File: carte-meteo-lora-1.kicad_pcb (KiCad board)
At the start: 2 copper layers, 60 x 45 mm, 121 parts, among them J1 TC2030, J2 Conn_01x04, J3 Conn_01x04, J4 Conn_Coaxial, J5 USB_C_Receptacle_USB2.0_14P, J6 Solar_Cell, J7 Conn_01x02, J8 Battery_Cell, Q1 AO4882, Q2 AO4882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

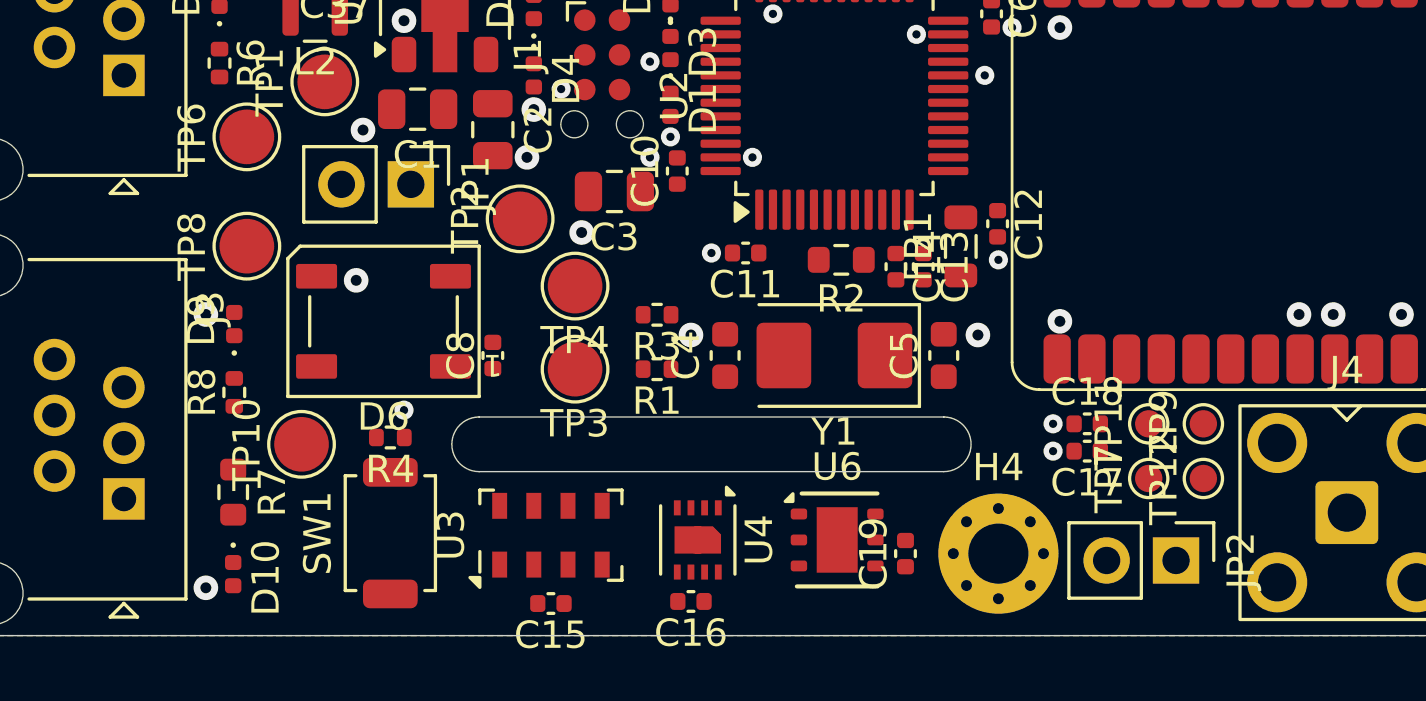
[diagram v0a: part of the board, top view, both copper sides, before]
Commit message: pcb: reorganize programmable gpios
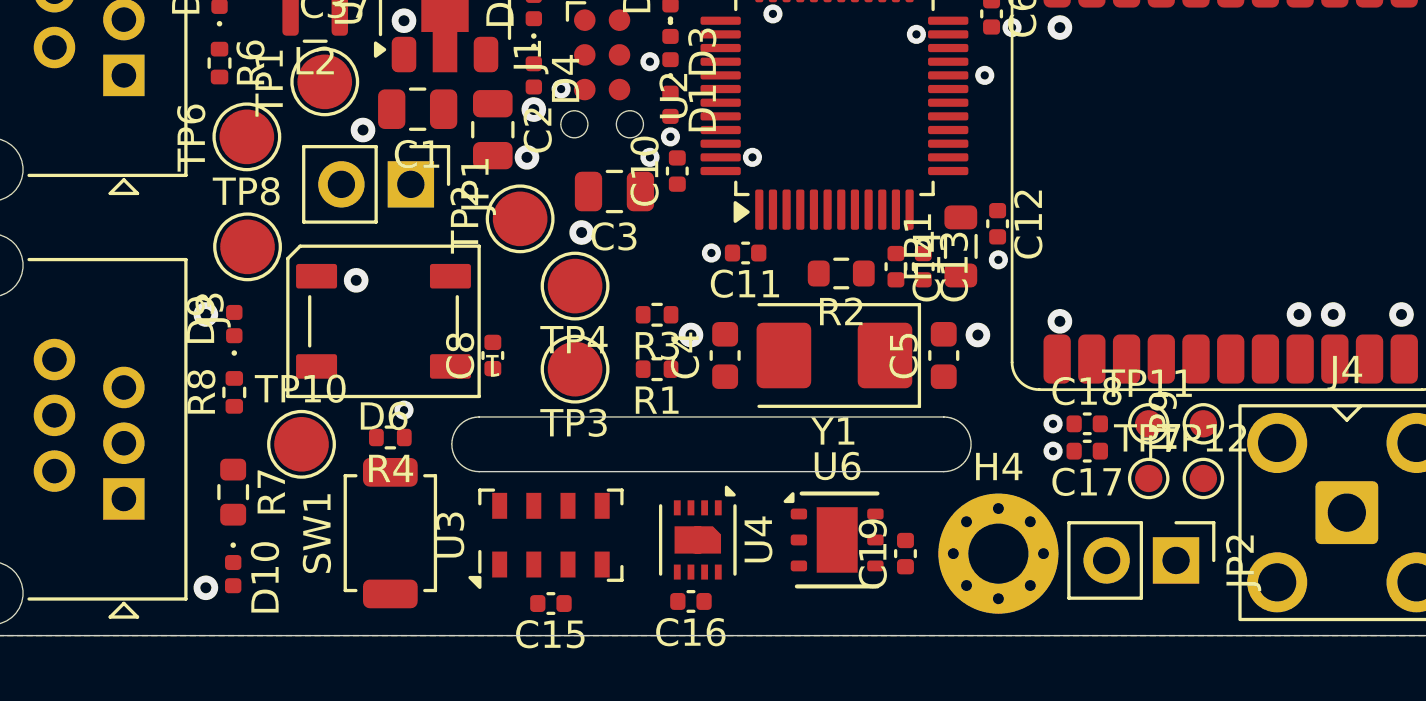
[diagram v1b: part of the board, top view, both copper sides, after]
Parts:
- moved R2 0.50 mm to (87.2, 54.8)
- turned TP8 to 0 degrees
- turned TP10 to 0 degrees
- turned TP11 to 0 degrees
- turned TP12 to 0 degrees
- turned TP7 to 0 degrees
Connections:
- R5 pad 1: Net-(U2-PA15) -> Net-(U2-PB12)
- U2 pad 10: /RAIN -> /WIND
- U2 pad 11: /SCK -> /W_DIR
- U2 pad 12: /WIND -> /ALERT
- U2 pad 15: /W_DIR -> /SCK
- U2 pad 16: /RGB1 -> /MISO
- U2 pad 17: unconnected-(U2-PA7-Pad17) -> /MOSI
- U2 pad 18: unconnected-(U2-PB0-Pad18) -> /RST
- U2 pad 19: unconnected-(U2-PB1-Pad19) -> /DIO1
- U2 pad 2: unconnected-(U2-PC13-Pad2) -> /RGB1
- U2 pad 21: /Power/~{CE} -> /DIO3
- U2 pad 22: unconnected-(U2-PB11-Pad22) -> /BUSY
- U2 pad 25: /RST -> Net-(U2-PB12)
- U2 pad 26: /DIO3 -> /BTN1
- U2 pad 27: /DIO1 -> unconnected-(U2-PB14-Pad27)
- U2 pad 28: /BUSY -> unconnected-(U2-PB15-Pad28)
- U2 pad 30: /ALERT -> unconnected-(U2-PA9-Pad30)
- U2 pad 31: unconnected-(U2-PA10-Pad31) -> /Power/~{QON}
- U2 pad 32: /MISO -> /Power/~{CE}
- U2 pad 33: /MOSI -> /Power/~{INT}
- U2 pad 38: Net-(U2-PA15) -> unconnected-(U2-PA15-Pad38)
- U2 pad 40: unconnected-(U2-PB4-Pad40) -> /RAIN
- U2 pad 41: /BTN1 -> unconnected-(U2-PB5-Pad41)
- U2 pad 45: /Power/~{QON} -> unconnected-(U2-PB8-Pad45)
- U2 pad 46: /Power/~{INT} -> unconnected-(U2-PB9-Pad46)

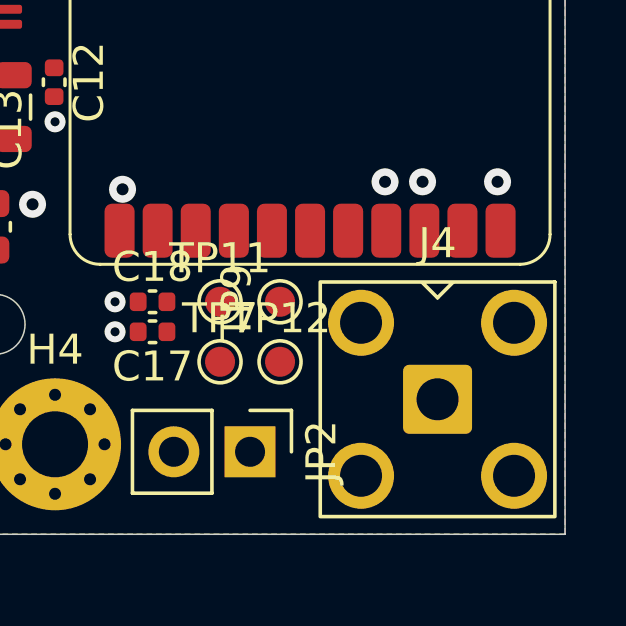
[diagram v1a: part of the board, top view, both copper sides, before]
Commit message: pcb: add rf routing
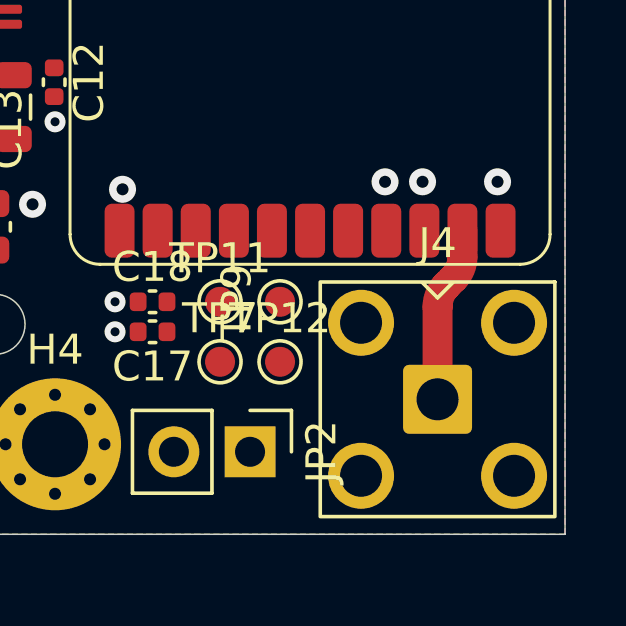
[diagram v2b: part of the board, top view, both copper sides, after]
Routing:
- net /RF_LR: track 0.00 -> 5.87 mm
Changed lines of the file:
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@@
 		(net "GND")
+	)
+	(segment
+		(start 106.58 57.88)
+		(end 106.58 58.755786)
+		(width 1)
+		(layer "F.Cu")
+		(net "/RF_LR")
+	)
+	(segment
+		(start 105.75 60.414172)
+		(end 105.75 63.5)
+		(width 1)
+		(layer "F.Cu")
+		(net "/RF_LR")
+	)
+	(segment
+		(start 106.287138 59.462862)
+		(end 106.042893 59.707107)
+		(width 1)
+		(layer "F.Cu")
+		(net "/RF_LR")
+	)
+	(arc
+		(start 106.287138 59.462862)
+		(mid 106.503891 59.138465)
+		(end 106.58 58.755786)
+		(width 1)
+		(layer "F.Cu")
+		(net "/RF_LR")
+	)
+	(arc
+		(start 106.042893 59.707107)
+		(mid 105.826125 60.031498)
+		(end 105.75 60.414172)
+		(width 1)
+		(layer "F.Cu")
+		(net "/RF_LR")
 	)
 	(zone

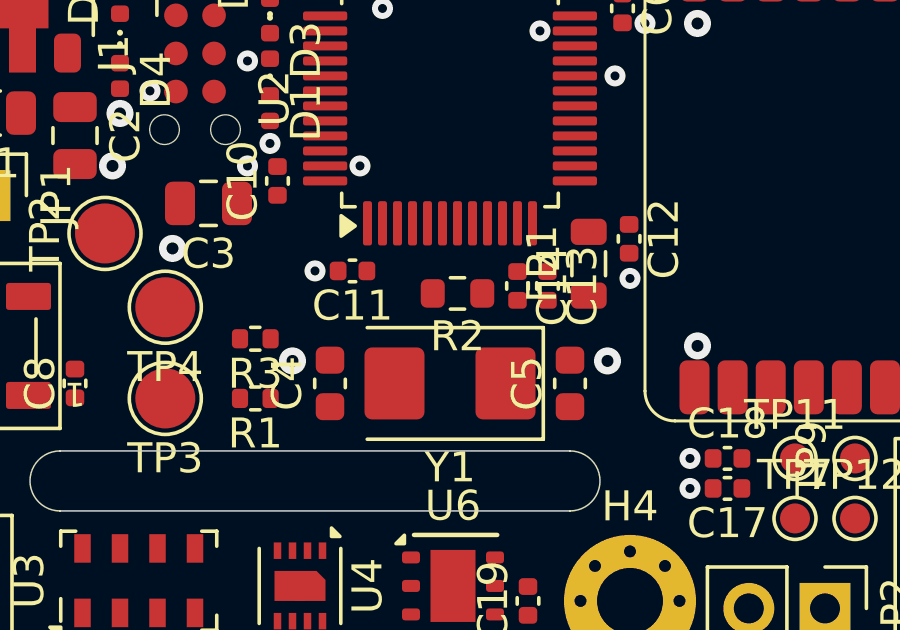
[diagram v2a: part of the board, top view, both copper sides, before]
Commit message: pcb: add xtal routing
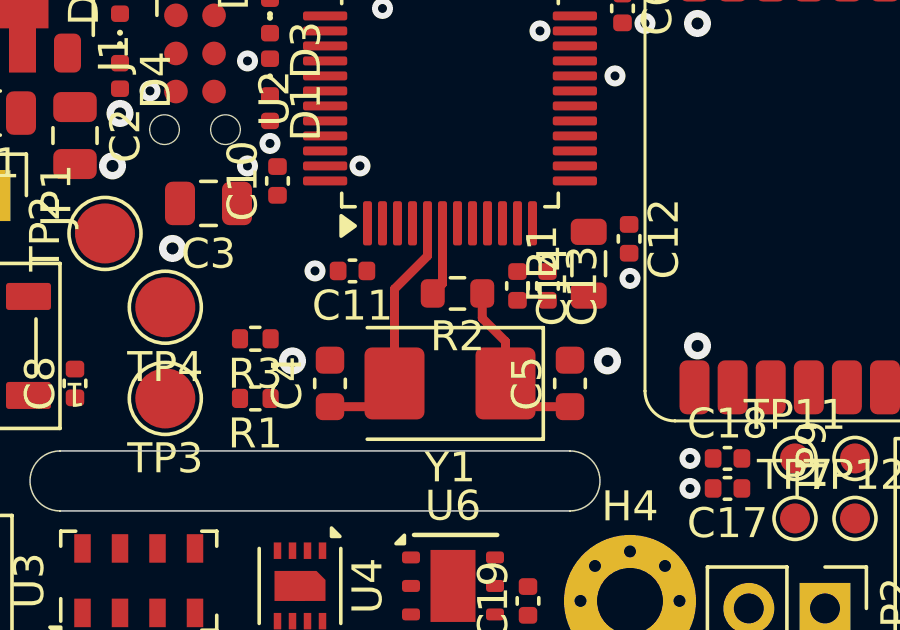
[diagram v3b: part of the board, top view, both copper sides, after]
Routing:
- net /XTAL_I: track 0.00 -> 8.26 mm
- net /XTAL_RO: track 0.00 -> 5.79 mm
- net /XTAL_O: track 0.00 -> 2.47 mm
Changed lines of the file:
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@@
+	)
+	(segment
+		(start 88.85 57.75)
+		(end 88.85 56.35)
+		(width 0.3)
+		(layer "F.Cu")
+		(net "/XTAL_RO")
+	)
+	(segment
+		(start 88.85 56.35)
+		(end 88.075 55.575)
+		(width 0.3)
+		(layer "F.Cu")
+		(net "/XTAL_RO")
+	)
+	(segment
+		(start 88.075 55.575)
+		(end 88.075 54.75)
+		(width 0.3)
+		(layer "F.Cu")
+		(net "/XTAL_RO")
+	)
+	(segment
+		(start 89.625 58.525)
+		(end 88.85 57.75)
+		(width 0.3)
+		(layer "F.Cu")
+		(net "/XTAL_RO")
+	)
+	(segment
+		(start 91 58.525)
+		(end 89.625 58.525)
+		(width 0.3)
+		(layer "F.Cu")
+		(net "/XTAL_RO")
 	)
 	(segment
@@
 	)
 	(segment
+		(start 83 58.525)
+		(end 84.375 58.525)
+		(width 0.3)
+		(layer "F.Cu")
+		(net "/XTAL_I")
+	)
+	(segment
+		(start 84.375 58.525)
+		(end 85.15 57.75)
+		(width 0.3)
+		(layer "F.Cu")
+		(net "/XTAL_I")
+	)
+	(segment
+		(start 86.25 52.4125)
+		(end 86.25 53.5)
+		(width 0.3)
+		(layer "F.Cu")
+		(net "/XTAL_I")
+	)
+	(segment
+		(start 86.25 53.5)
+		(end 85.15 54.6)
+		(width 0.3)
+		(layer "F.Cu")
+		(net "/XTAL_I")
+	)
+	(segment
+		(start 85.15 54.6)
+		(end 85.15 57.75)
+		(width 0.3)
+		(layer "F.Cu")
+		(net "/XTAL_I")
+	)
+	(segment
+		(start 86.75 52.4125)
+		(end 86.75 54.425)
+		(width 0.3)
+		(layer "F.Cu")
+		(net "/XTAL_O")
+	)
+	(segment
+		(start 86.75 54.425)
+		(end 86.425 54.75)
+		(width 0.3)
+		(layer "F.Cu")
+		(net "/XTAL_O")
+	)
+	(segment

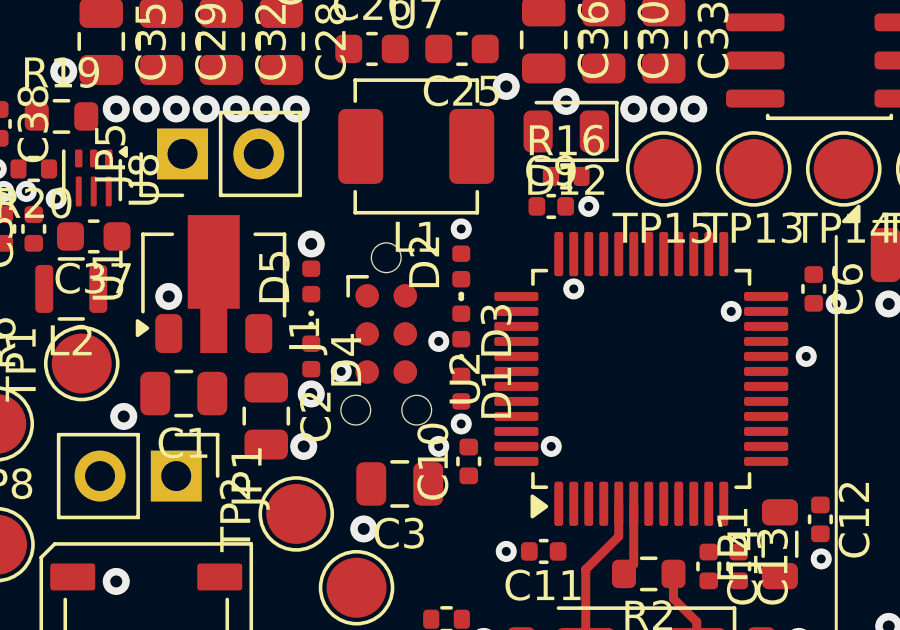
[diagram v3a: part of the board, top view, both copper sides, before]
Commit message: pcb: add swd routing
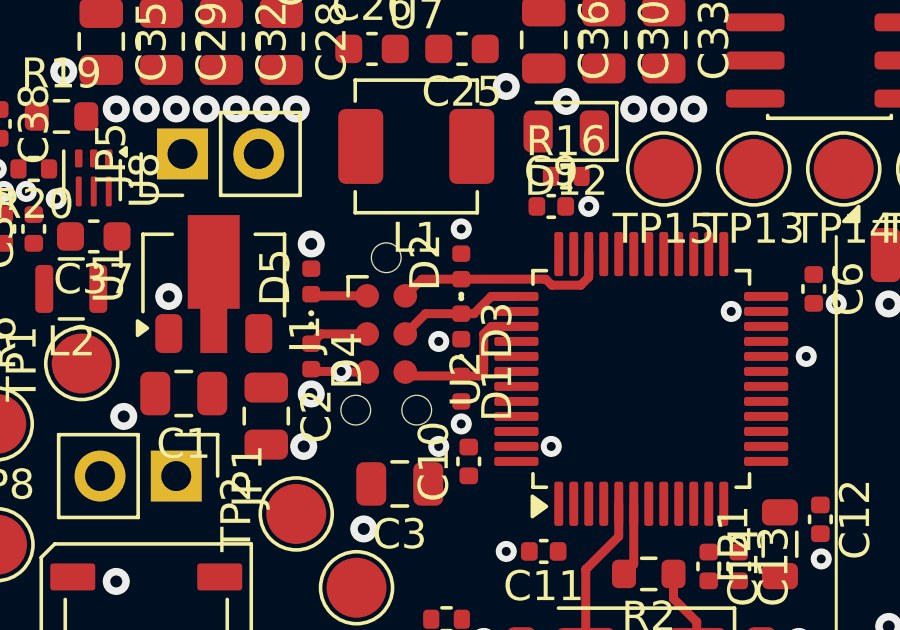
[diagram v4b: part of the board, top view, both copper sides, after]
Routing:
- net /SWDIO: track 0.00 -> 7.31 mm
- net /SWO: track 0.00 -> 5.17 mm
- net /SWCLK: track 0.00 -> 4.22 mm
- net /NRST: track 0.00 -> 2.00 mm
- net GND: track 1.45 -> 3.36 mm, vias 73 -> 72
- net +3V3: track 0.00 -> 1.89 mm
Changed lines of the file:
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@@
+	)
+	(segment
+		(start 76.075 48)
+		(end 76 47.925)
+		(width 0.3)
+		(layer "F.Cu")
+		(net "GND")
 	)
 	(segment
@@
 	)
 	(segment
+		(start 77.02 48.02)
+		(end 77 48)
+		(width 0.3)
+		(layer "F.Cu")
+		(net "GND")
+	)
+	(segment
+		(start 77 48)
+		(end 76.075 48)
+		(width 0.3)
+		(layer "F.Cu")
+		(net "GND")
+	)
+	(segment
 		(start 76.96 27.75)
 		(end 77 27.75)
@@
 		(net "GND")
 	)
+	(segment
+		(start 77.865 48.02)
+		(end 77.02 48.02)
+		(width 0.3)
+		(layer "F.Cu")
+		(net "GND")
+	)
 	(via
 		(at 100.18 29.51)
@@
 	)
 	(via
-		(at 84.75 45.25)
-		(size 0.7)
-		(drill 0.3)
-		(layers "F.Cu" "B.Cu")
-		(free yes)
-		(net "GND")
-	)
-	(via
 		(at 80.25 47)
 		(size 0.7)
@@
 		(free yes)
 		(net "GND")
+	)
+	(segment
+		(start 76.055 45.48)
+		(end 76 45.425)
+		(width 0.3)
+		(layer "F.Cu")
+		(net "+3V3")
+	)
+	(segment
+		(start 77.865 45.48)
+		(end 76.055 45.48)
+		(width 0.3)
+		(layer "F.Cu")
+		(net "+3V3")
+	)
+	(segment
+		(start 82.8375 45.5)
+		(end 82 45.5)
+		(width 0.3)
+		(layer "F.Cu")
+		(net "/SWCLK")
+	)
+	(segment
+		(start 79.81 46.075)
+		(end 79.135 46.75)
+		(width 0.3)
+		(layer "F.Cu")
+		(net "/SWCLK")
+	)
+	(segment
+		(start 82 45.5)
+		(end 81.425 46.075)
+		(width 0.3)
+		(layer "F.Cu")
+		(net "/SWCLK")
+	)
+	(segment
+		(start 81.425 46.075)
+		(end 81 46.075)
+		(width 0.3)
+		(layer "F.Cu")
+		(net "/SWCLK")
+	)
+	(segment
+		(start 81 46.075)
+		(end 79.81 46.075)
+		(width 0.3)
+		(layer "F.Cu")
+		(net "/SWCLK")
 	)
 	(segment
@@
 	)
 	(segment
+		(start 76.325 46.75)
+		(end 76 47.075)
+		(width 0.3)
+		(layer "F.Cu")
+		(net "/NRST")
+	)
+	(segment
+		(start 77.865 46.75)
+		(end 76.325 46.75)
+		(width 0.3)
+		(layer "F.Cu")
+		(net "/NRST")
+	)
+	(segment
+		(start 81 44.925)
+		(end 79.69 44.925)
+		(width 0.3)
+		(layer "F.Cu")
+		(net "/SWDIO")
+	)
+	(segment
+		(start 83.81759 44.925)
+		(end 84.01759 45.125)
+		(width 0.3)
+		(layer "F.Cu")
+		(net "/SWDIO")
+	)
+	(segment
+		(start 81 44.925)
+		(end 83.81759 44.925)
+		(width 0.3)
+		(layer "F.Cu")
+		(net "/SWDIO")
+	)
+	(segment
+		(start 84.01759 45.125)
+		(end 84.98241 45.125)
+		(width 0.3)
+		(layer "F.Cu")
+		(net "/SWDIO")
+	)
+	(segment
+		(start 84.98241 45.125)
+		(end 85.25 44.85741)
+		(width 0.3)
+		(layer "F.Cu")
+		(net "/SWDIO")
+	)
+	(segment
+		(start 85.25 44.85741)
+		(end 85.25 44.0875)
+		(width 0.3)
+		(layer "F.Cu")
+		(net "/SWDIO")
+	)
+	(segment
+		(start 79.69 44.925)
+		(end 79.135 45.48)
+		(width 0.3)
+		(layer "F.Cu")
+		(net "/SWDIO")
+	)
+	(segment
+		(start 82 46.5)
+		(end 81.75 46.75)
+		(width 0.3)
+		(layer "F.Cu")
+		(net "/SWO")
+	)
+	(segment
+		(start 82.8375 46.5)
+		(end 82 46.5)
+		(width 0.3)
+		(layer "F.Cu")
+		(net "/SWO")
+	)
+	(segment
+		(start 81.75 46.75)
+		(end 81.75 48)
+		(width 0.3)
+		(layer "F.Cu")
+		(net "/SWO")
+	)
+	(segment
+		(start 79.265 48.15)
+		(end 79.135 48.02)
+		(width 0.3)
+		(layer "F.Cu")
+		(net "/SWO")
+	)
+	(segment
+		(start 81.6 48.15)
+		(end 81 48.15)
+		(width 0.3)
+		(layer "F.Cu")
+		(net "/SWO")
+	)
+	(segment
+		(start 81.75 48)
+		(end 81.6 48.15)
+		(width 0.3)
+		(layer "F.Cu")
+		(net "/SWO")
+	)
+	(segment
+		(start 81 48.15)
+		(end 79.265 48.15)
+		(width 0.3)
+		(layer "F.Cu")
+		(net "/SWO")
+	)
+	(segment

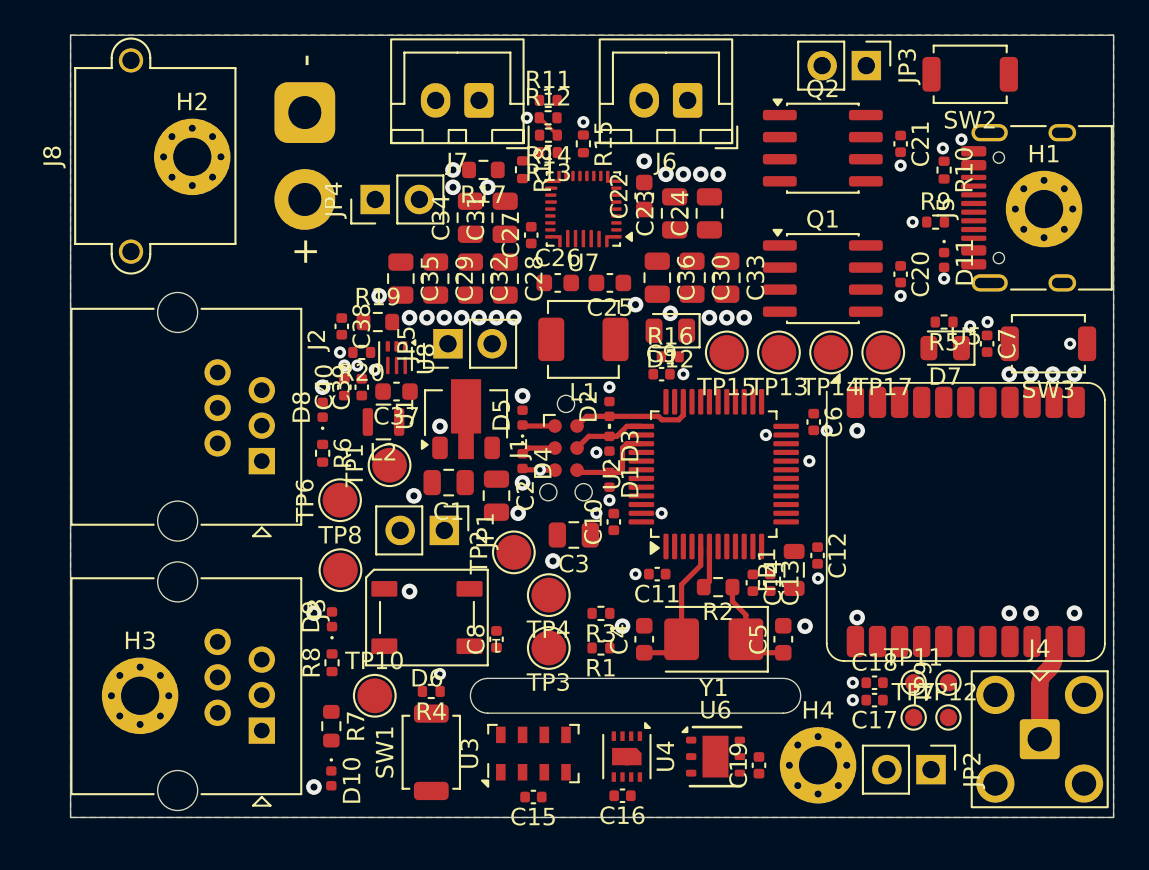
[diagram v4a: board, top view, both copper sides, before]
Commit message: pcb: add i2c routing
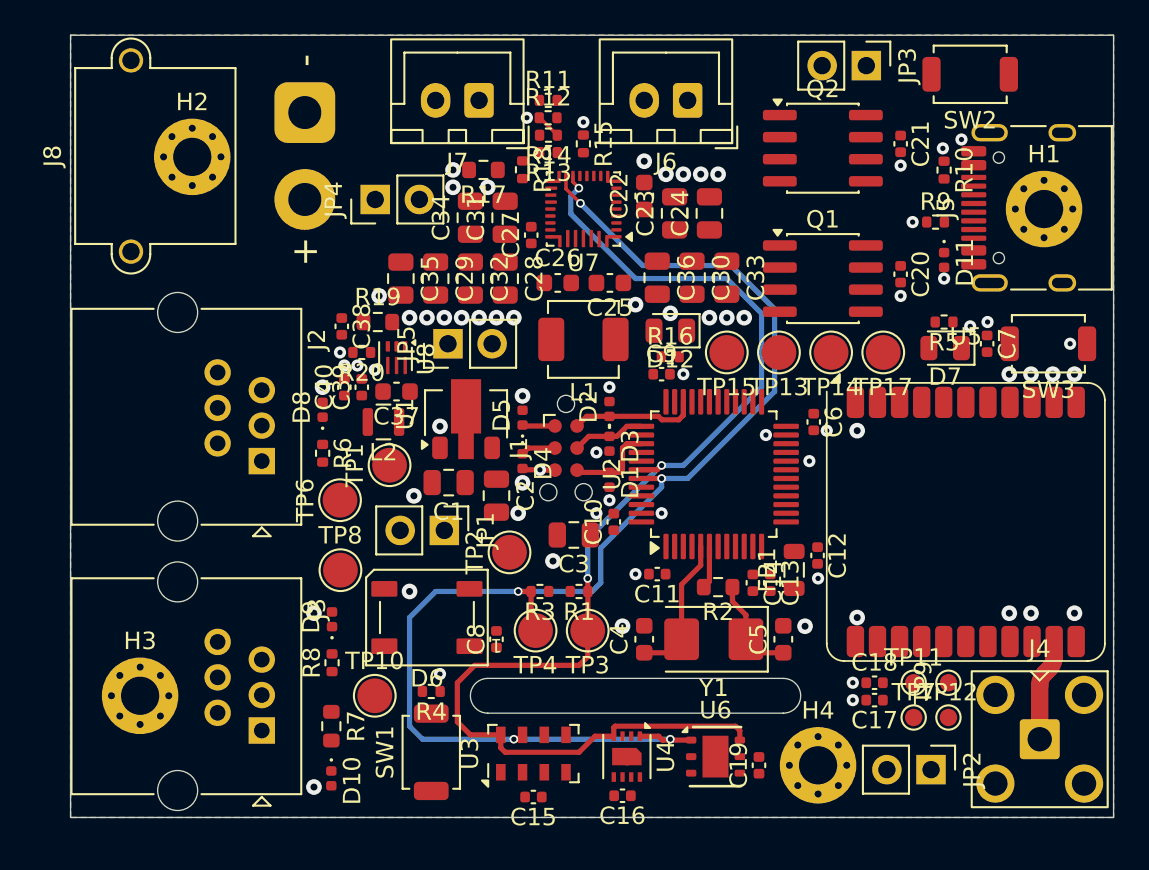
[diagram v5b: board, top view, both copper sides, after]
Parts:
- moved R3 3.73 mm to (77.0, 55.0)
- moved R1 3.49 mm to (79.2, 55.0)
- moved TP3 2.45 mm to (79.8, 57.2)
- moved TP4 2.18 mm to (76.8, 57.2)
- moved TP2 0.25 mm to (75.2, 52.8)
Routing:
- net /SDA: track 0.00 -> 77.7 mm, vias 0 -> 5
- net /SCL: track 0.00 -> 71.1 mm, vias 0 -> 3
